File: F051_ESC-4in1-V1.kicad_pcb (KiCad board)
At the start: 4 copper layers, 46 x 55.8 mm, 222 parts, among them J1 Conn_01x02, J11 Conn_01x03, J14 Conn_01x03, J2 Conn_01x10, J3 Conn_01x05, J4 Conn_01x05, J5 Conn_01x05, J6 Conn_01x03, J7 Conn_01x05, J8 Conn_01x03, J9 Conn_01x10, Q1 TPHR8504PL, Q10 TPHR8504PL, Q11 TPHR8504PL, Q12 TPHR8504PL, Q13 TPHR8504PL, Q14 TPHR8504PL, Q15 TPHR8504PL, Q16 TPHR8504PL, Q17 TPHR8504PL, Q18 TPHR8504PL, Q19 TPHR8504PL, Q2 TPHR8504PL, Q20 TPHR8504PL, Q21 TPHR8504PL, Q22 TPHR8504PL, Q23 TPHR8504PL, Q24 TPHR8504PL, Q3 TPHR8504PL, Q4 TPHR8504PL, Q5 TPHR8504PL, Q6 TPHR8504PL, Q7 TPHR8504PL, Q8 TPHR8504PL, Q9 TPHR8504PL, U1 STM32F051K6Ux, U10 FD6288Q, U11 STM32F051K6Ux, U12 FD6288Q, U13 L78L12_SOT89, U14 MP4560_QFN10, U2 FD6288Q, U3 L78L12_SOT89, U4 LP2985-3.3, U5 INA139, U6 FD6288Q, U7 OPA340NA, U8 STM32F051K6Ux, U9 STM32F051K6Ux

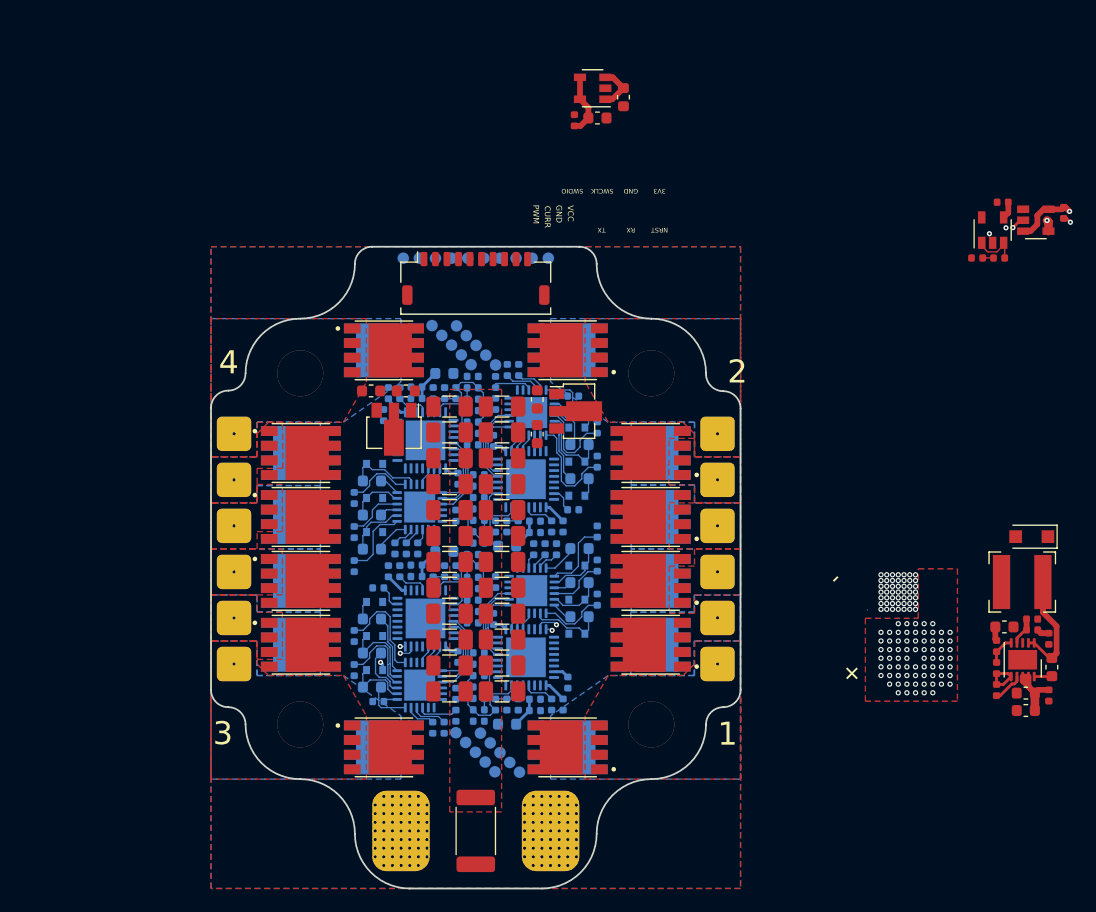
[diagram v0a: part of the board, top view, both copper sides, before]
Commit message: Added more planes, rearranged 5V circuit
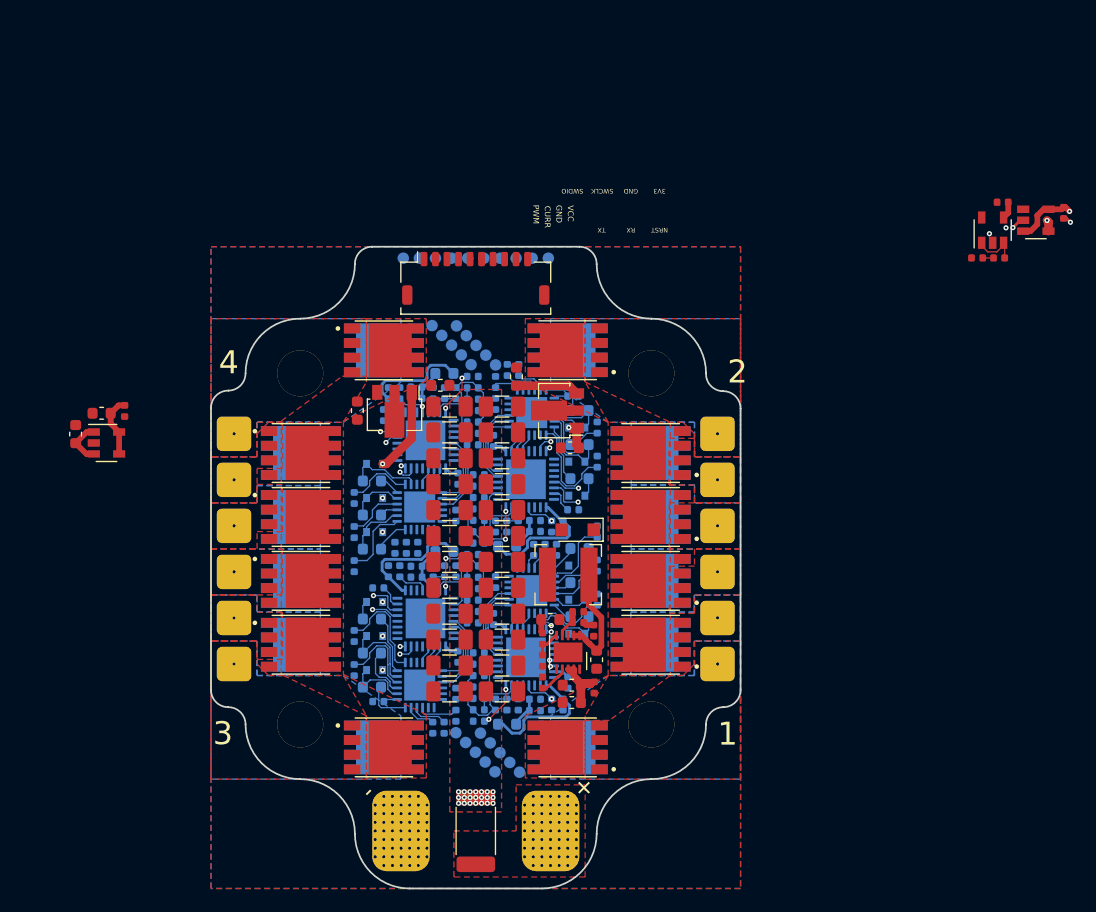
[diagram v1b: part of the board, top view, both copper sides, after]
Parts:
- moved C22 55.9 mm to (105.2, 78.5), turned to 90 degrees
- moved U4 52.3 mm to (107.9, 79.3), turned to 0 degrees
- moved C24 50.1 mm to (107.5, 76.7), turned to 180 degrees
- moved C23 46.5 mm to (109.5, 76.5), turned to 270 degrees
- moved R77 39.5 mm to (150.2, 95.6)
- moved C70 39.5 mm to (150.5, 98.1)
- moved C74 39.5 mm to (150.3, 100.5)
- moved U14 39.5 mm to (148.0, 97.5)
- moved C72 39.4 mm to (148.3, 101.8)
- moved C73 39.4 mm to (148.3, 100.3)
- moved C75 39.4 mm to (148.9, 94.9)
- moved C76 39.4 mm to (148.9, 94.0)
- moved C71 39.4 mm to (146.5, 94.6)
- moved L1 39.4 mm to (148.0, 90.7)
- moved R73 39.4 mm to (145.8, 96.3)
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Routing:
- net +3V3: track 18.2 -> 54.5 mm
- net +12V: track 0.76 -> 9.26 mm, vias 1 -> 7
- net VCC_Shunt: track 7.87 -> 14.9 mm, vias 50 -> 22
- net Net-(R31-Pad1): track 0.00 -> 4.78 mm, vias 0 -> 2
- net Net-(R42-Pad1): track 0.00 -> 4.77 mm, vias 0 -> 2
- net Net-(R59-Pad1): track 0.00 -> 4.06 mm, vias 0 -> 2
- net Net-(R11-Pad1): track 0.00 -> 4.02 mm, vias 0 -> 2
- net GND: track 5.75 -> 1.88 mm
- net /MCU 3/USART1_RX: track 0.00 -> 3.14 mm, vias 0 -> 1
- net /MCU 2/USART1_RX: track 0.00 -> 3.13 mm, vias 0 -> 1
- net /MCU 3/USART1_TX: track 0.00 -> 2.38 mm, vias 0 -> 1
- net /MCU 2/USART1_TX: track 0.00 -> 2.35 mm, vias 0 -> 1
- net /MOSFET Driver 4/LO1: track 2.00 -> 0.00 mm
- net +3.3VA: track 10.6 -> 12.2 mm
- net /MCU 4/SWDIO: track 0.00 -> 1.57 mm, vias 0 -> 1
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
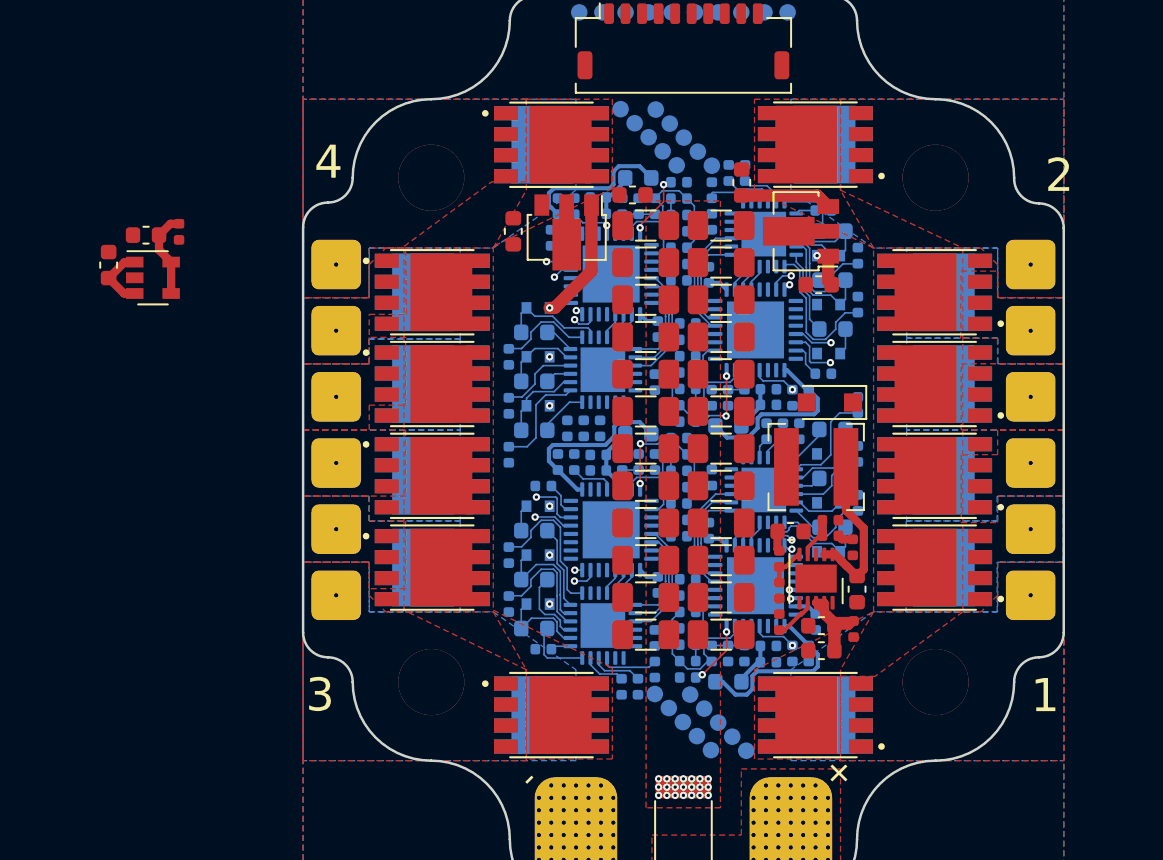
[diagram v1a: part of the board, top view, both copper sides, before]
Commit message: Added 3V3 regulator and connected it to rest of board
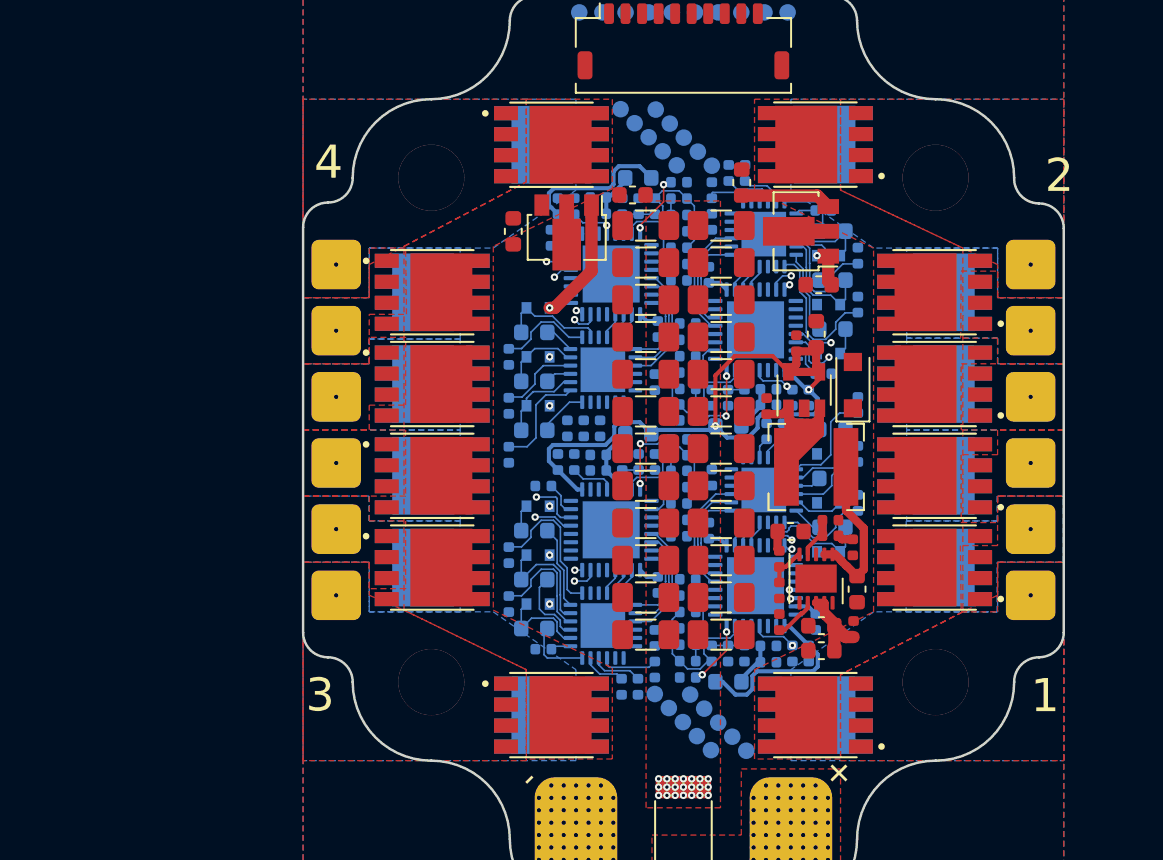
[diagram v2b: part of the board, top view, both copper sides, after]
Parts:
- C22: footprint Capacitor_SMD:C_0603_1608Metric -> Capacitor_SMD:C_0402_1005Metric
- moved C24 41.0 mm to (148.0, 82.7), turned to 90 degrees
- moved C22 40.7 mm to (145.0, 87.1)
- moved U4 40.0 mm to (147.3, 86.1), turned to 90 degrees
- moved C23 37.9 mm to (146.8, 83.3), turned to 90 degrees
- moved D13 1.74 mm to (150.2, 85.8), turned to 90 degrees
- moved R31 0.08 mm to (140.3, 87.9)
- moved R42 0.08 mm to (139.7, 89.1)
- moved R30 0.05 mm to (140.3, 87.0)
- turned C74 to 90 degrees
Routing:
- net +3V3: track 54.5 -> 69.1 mm, vias 0 -> 2
- net +5V: track 5.17 -> 18.1 mm
- net VCC_Shunt: track 14.9 -> 13.9 mm
- added copper zone on In2.Cu, net +3V3
- added copper zone on F.Cu, net /MCU 1/PhaseB

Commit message: Connected a lot of stuff
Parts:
- removed C7: 0.1uF, Capacitor_SMD:C_0402_1005Metric
- removed C8: 3.3nF, Capacitor_SMD:C_0402_1005Metric
- removed R2: 60k, Resistor_SMD:R_0402_1005Metric
- removed R3: 500, Resistor_SMD:R_0402_1005Metric
- moved U5 7.93 mm to (182.3, 55.2)
- moved U7 3.14 mm to (182.1, 59.5)
- moved R26 1.69 mm to (143.2, 73.1)
- moved FB1 1.55 mm to (144.3, 103.7), turned to 0 degrees
- moved Q1 1.50 mm to (149.5, 105.8)
- moved Q11 1.50 mm to (149.5, 71.2)
- moved Q12 1.50 mm to (149.5, 71.2)
- moved Q17 1.50 mm to (130.5, 105.8)
- moved Q18 1.50 mm to (130.5, 105.8)
- moved Q19 1.50 mm to (130.5, 71.3)
- moved Q2 1.50 mm to (149.5, 105.8)
- moved Q20 1.50 mm to (130.5, 71.3)
- moved R5 1.41 mm to (145.1, 73.1)
- moved R22 1.41 mm to (144.1, 73.1)
- moved R24 0.75 mm to (145.6, 88.1), turned to 180 degrees
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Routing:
- net /MCU 2/PhaseB: track 4.49 -> 55.8 mm, vias 0 -> 4
- net /MCU 1/PhaseC: track 3.37 -> 54.5 mm, vias 0 -> 2
- net /MCU 2/PhaseC: track 4.74 -> 52.1 mm, vias 0 -> 2
- net /PWM_1: track 0.00 -> 45.7 mm, vias 0 -> 4
- net /MCU 1/PhaseB: track 1.59 -> 40.8 mm, vias 0 -> 2
- net /MCU 2/PhaseA: track 5.46 -> 43.7 mm, vias 0 -> 2
- net /MCU 1/PhaseA: track 1.82 -> 36.6 mm, vias 0 -> 2
- net /PWM_2: track 0.00 -> 31.8 mm, vias 0 -> 2
- net +5V: track 18.1 -> 48.0 mm, vias 0 -> 4
- net +12V: track 9.26 -> 37.4 mm, vias 7 -> 12
- net Net-(Q2-Pad4): track 0.00 -> 23.7 mm
- net Net-(Q20-Pad4): track 0.00 -> 23.0 mm
- net /MCU 1/SWCLK: track 0.54 -> 20.6 mm, vias 1 -> 2
- net /MCU 1/SWDIO: track 1.62 -> 19.8 mm, vias 1 -> 2
- net Net-(Q8-Pad4): track 0.00 -> 16.6 mm
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
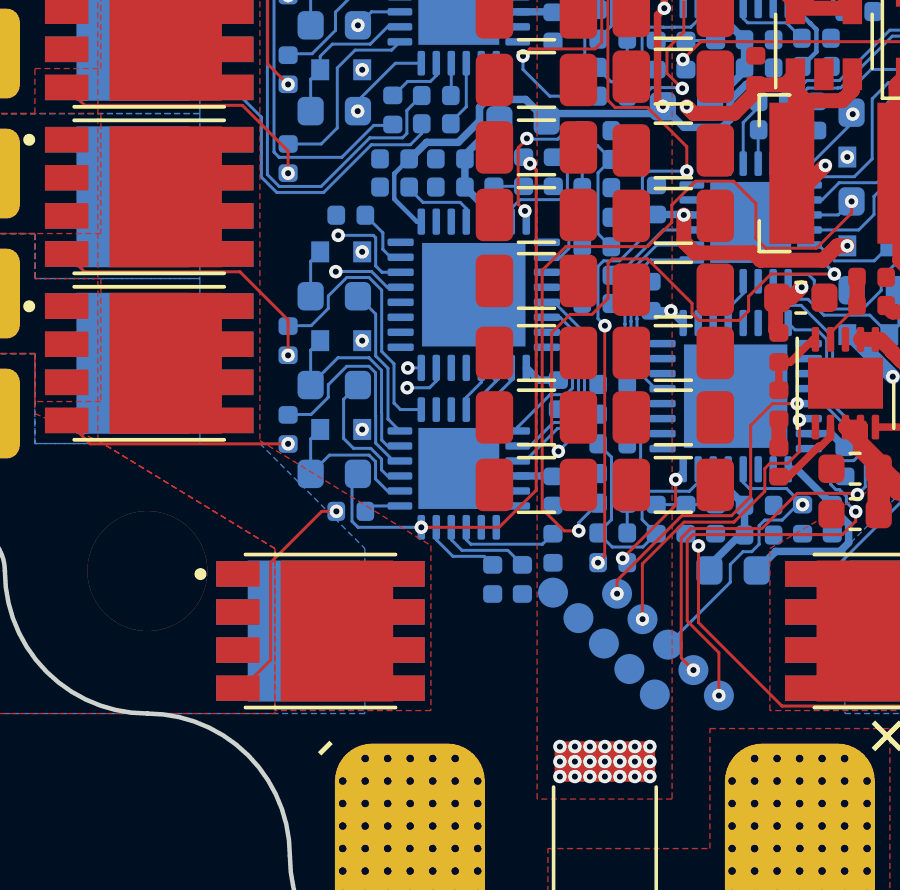
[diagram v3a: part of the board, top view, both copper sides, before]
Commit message: A few more traces laid out
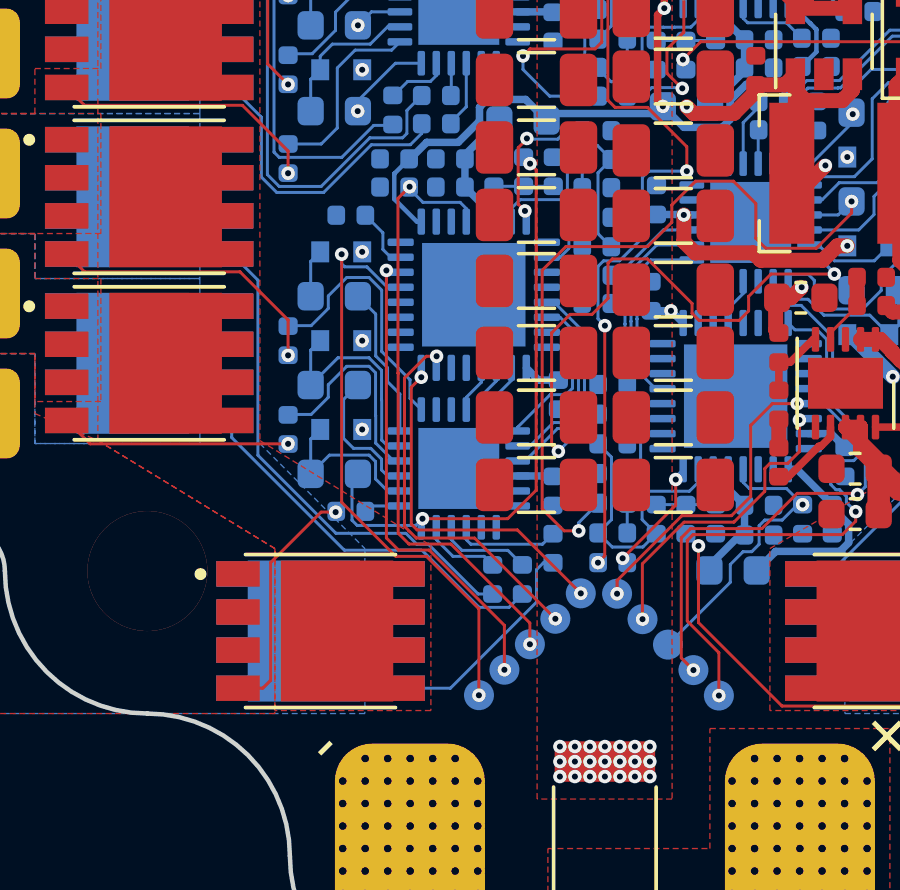
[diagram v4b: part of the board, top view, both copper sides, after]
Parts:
- moved J4 2.47 mm to (137.5, 106.2), turned to 225 degrees
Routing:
- net /MCU 3/NRST: track 2.72 -> 20.8 mm, vias 0 -> 2
- net /MCU 3/USART1_TX: track 2.38 -> 19.8 mm, vias 1 -> 2
- net Net-(Q14-Pad4): track 0.00 -> 16.8 mm
- net Net-(Q16-Pad4): track 0.00 -> 12.8 mm
- net /MCU 3/USART1_RX: track 3.14 -> 15.5 mm, vias 1 -> 2
- net /MCU 3/SWDIO: track 1.50 -> 13.0 mm, vias 1 -> 2
- net /MCU 3/SWCLK: track 0.45 -> 12.0 mm, vias 1 -> 2
- net Net-(Q18-Pad4): track 0.00 -> 7.36 mm
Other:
- board text added: "Think about flipping the sense “rows”(3). Might make routing the phases easier"

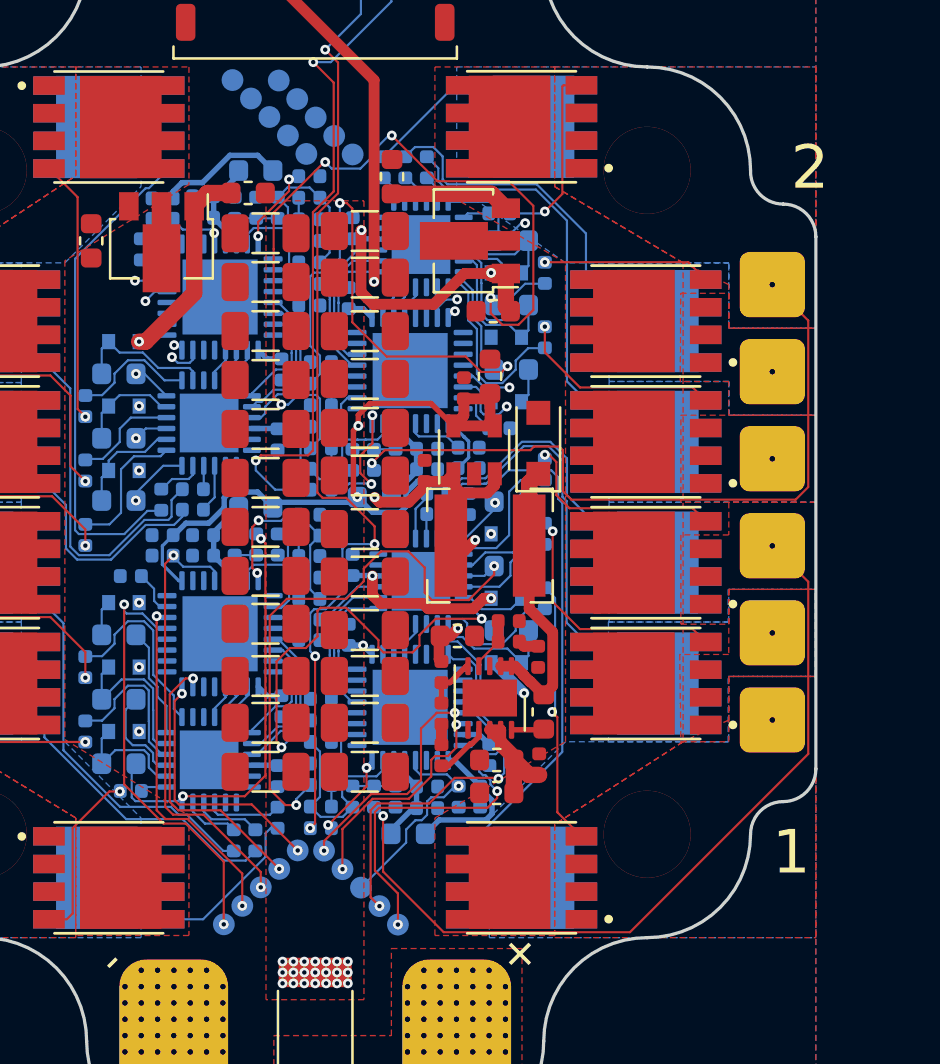
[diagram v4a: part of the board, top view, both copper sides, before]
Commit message: Rerouted a bunch of the phase traces so they are shorter
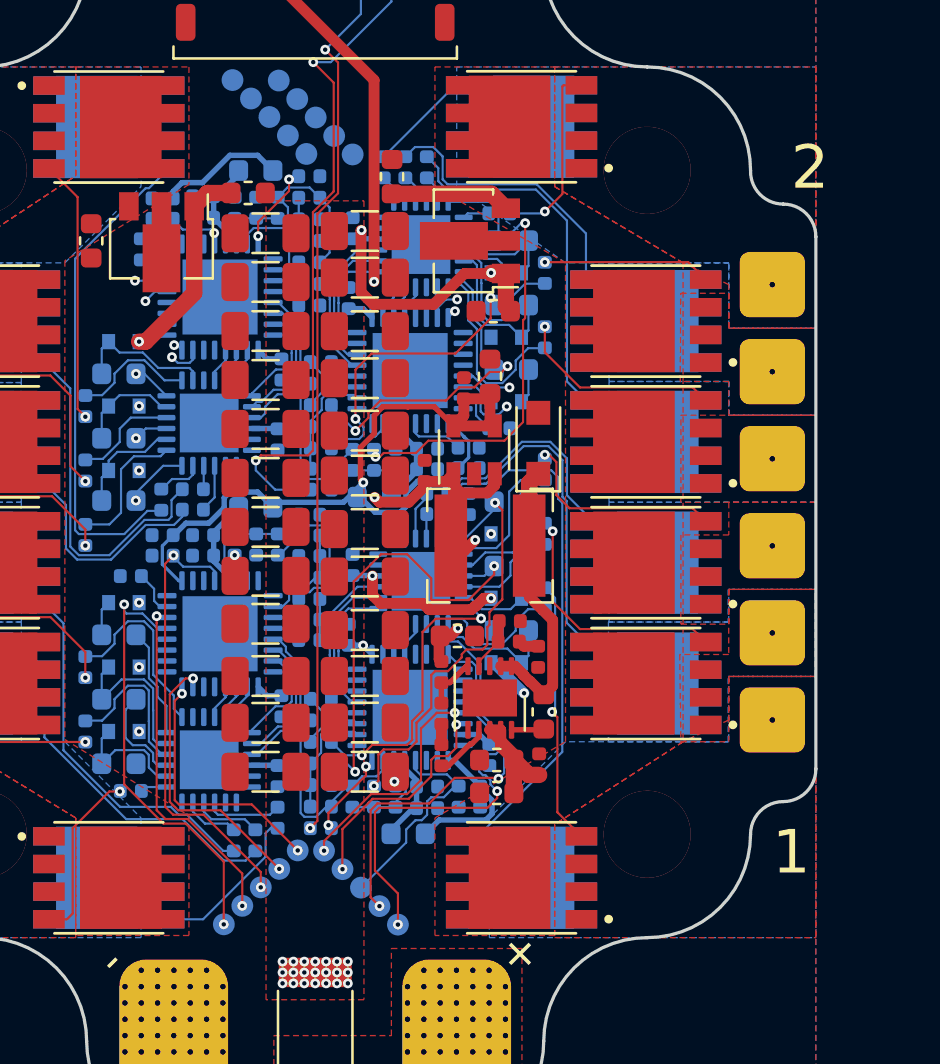
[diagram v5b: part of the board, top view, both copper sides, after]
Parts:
- moved R27 0.99 mm to (140.3, 84.0), turned to 0 degrees
- moved R28 0.99 mm to (140.3, 83.0)
- moved R7 0.99 mm to (140.3, 99.5), turned to 0 degrees
- moved R8 0.99 mm to (140.3, 98.5)
- moved R15 0.99 mm to (140.3, 101.5), turned to 180 degrees
- moved R9 0.99 mm to (140.3, 100.5), turned to 0 degrees
- moved C53 0.13 mm to (142.3, 85.2)
- moved C76 0.05 mm to (148.9, 94.0)
- turned R10 to 0 degrees
- turned R12 to 90 degrees
- turned R13 to 90 degrees
- turned R14 to 180 degrees
- turned R16 to 270 degrees
- turned R29 to 0 degrees
- turned R30 to 0 degrees
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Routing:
- net /MCU 2/PhaseB: track 55.8 -> 32.3 mm, vias 4 -> 2
- net /MCU 1/PhaseA: track 36.6 -> 14.4 mm
- net /MCU 1/PhaseC: track 54.5 -> 34.1 mm
- net /MCU 3/PhaseC: track 19.9 -> 0.34 mm, vias 2 -> 0
- net /MCU 2/PhaseC: track 52.1 -> 35.6 mm
- net /MCU 2/PhaseA: track 43.7 -> 30.1 mm
- net Net-(R31-Pad1): track 6.70 -> 0.00 mm, vias 2 -> 0
- net /MCU 1/PhaseB: track 40.8 -> 35.1 mm
- net Net-(R42-Pad1): track 4.99 -> 0.00 mm, vias 2 -> 0
- net /PWM_1: track 45.7 -> 41.7 mm, vias 4 -> 2
- net /MCU 3/SenseCOM: track 9.52 -> 7.25 mm
- net /MCU 3/SenseC: track 3.19 -> 4.55 mm
- net /MCU 1/SenseC: track 3.19 -> 4.55 mm
- net /MCU 3/SenseA: track 3.22 -> 1.89 mm
- net /MCU 1/SenseB: track 4.05 -> 5.28 mm
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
